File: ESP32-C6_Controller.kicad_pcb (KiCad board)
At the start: 6 copper layers, 30 x 50 mm, 54 parts, among them J1 USB4105-GF-A, J2 Conn_01x12, J3 Conn_01x12, SW1 SW_Push, SW2 SW_Push, U1 ESP32-C6, U2 W25Q16JVSSIQ, U3 AZ1117IH-3.3TRG1, U4 ESD122DMYR

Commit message: add comment to add fiducials
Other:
- board text added: "-Check DP1 and DN1 length? -why DP2 and DN2 -Increase trace width for power -add fiducials"
- board text removed: "-Check DP1 and DN1 length? -why DP2 and DN2 -Increase trace width for power"
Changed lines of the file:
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@@
 		)
 		(property "Value" "7.5M"
-			(at 0 1.17 360)
+			(at 0 1.17 0)
 			(layer "F.Fab")
 			(effects
@@
 		)
 		(fp_text user "${REFERENCE}"
-			(at 0 0 360)
+			(at 0 0 0)
 			(layer "F.Fab")
 			(effects
@@
 		)
 	)
-	(gr_text "-Check DP1 and DN1 length?\n-why DP2 and DN2\n-Increase trace width for power"
+	(gr_text "-Check DP1 and DN1 length?\n-why DP2 and DN2\n-Increase trace width for power\n-add fiducials"
 		(at 182.25 82.25 0)
 		(layer "User.6")

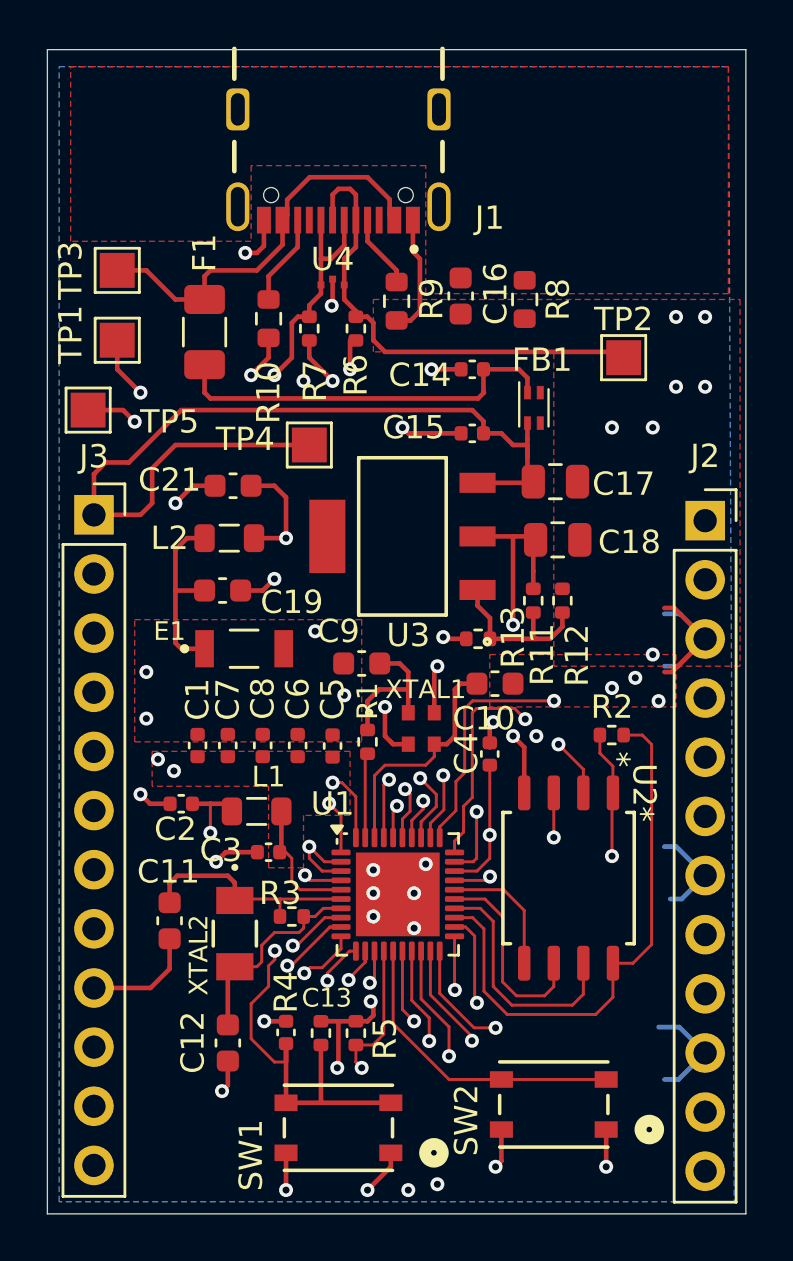
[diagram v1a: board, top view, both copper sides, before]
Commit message: fix unconnected and plane
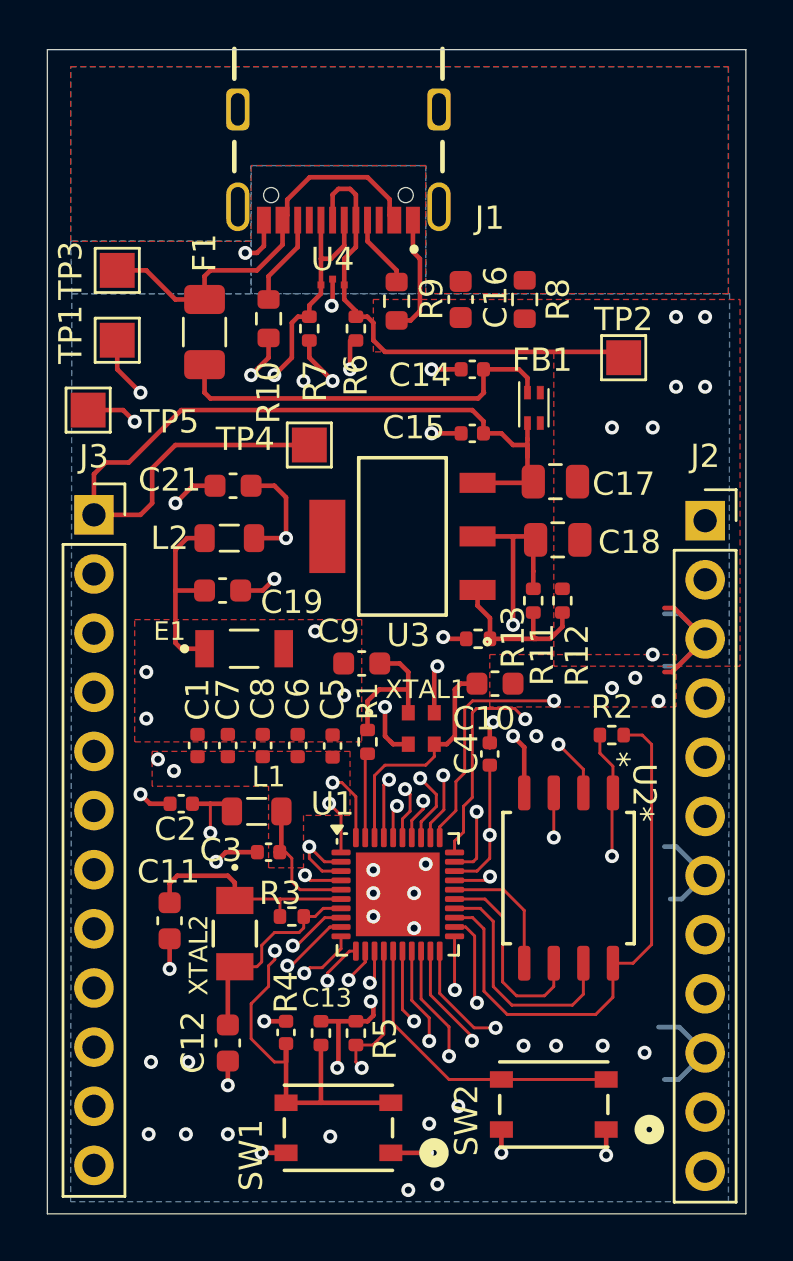
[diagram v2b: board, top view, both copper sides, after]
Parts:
- moved C16 0.15 mm to (158.0, 85.8)
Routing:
- net 3V3: track 44.4 -> 96.7 mm
- net GND: track 74.8 -> 54.7 mm, vias 39 -> 52
- added copper zone on In2.Cu, net GND
- added copper zone on In3.Cu, net GND
- added copper zone on In4.Cu, net GND
- added copper zone on B.Cu, net GND1
- added copper zone on In1.Cu, net GND1
- added copper zone on In2.Cu, net GND1
- added copper zone on In3.Cu, net GND1
- added copper zone on In4.Cu, net GND1
- removed copper zone on In4.Cu, net 3V3
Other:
- board text added: "0"
- board text added: "0 mm"
- board text added: "0.01 mm"
- board text added: "0.02"
- board text added: "0.035 mm"
- board text added: "0.1 mm"
- board text added: "0.535 mm"
- board text added: "1"
- board text added: "3.3"
- board text added: "4.5"
- board text added: "B.Cu"
- board text added: "B.Mask"
- board text added: "B.Paste"
- board text added: "B.Silkscreen"
- board text added: "Bottom Silk Screen"
- board text added: "Bottom Solder Mask"
- board text added: "Bottom Solder Paste"
- board text added: "Color"
- board text added: "Dielectric"
- board text added: "Epsilon R"
- board text added: "F.Cu"
- board text added: "F.Mask"
- board text added: "F.Paste"
- board text added: "F.Silkscreen"
- board text added: "FR4"
- board text added: "In1.Cu"
- board text added: "In2.Cu"
- board text added: "In3.Cu"
- board text added: "In4.Cu"
- board text added: "Layer Name"
- board text added: "Loss Tangent"
- board text added: "Material"
- board text added: "Not specified"
- board text added: "Thickness (mm)"
- board text added: "Top Silk Screen"
- board text added: "Top Solder Mask"
- board text added: "Top Solder Paste"
- board text added: "Type"
- board text added: "copper"
- board text added: "core"
- board text added: "prepreg"
